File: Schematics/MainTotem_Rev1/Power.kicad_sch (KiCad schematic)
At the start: 0 parts

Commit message: Adding the MTL Schematics in post editing
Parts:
- added 3V3HPSoC: YELLOW, symbol Device:LED
- added 3V3HSSoC: GREEN, symbol Device:LED
- added 3V3SoC, GND: TestPoint, symbol Connector:TestPoint
- added C33, C36, C37, C40: 10u, symbol Device:C
- added C34, C35, C38, C39: 100n, symbol Device:C
- added C41, C43: 4.7u, symbol Device:C
- added C42, C44, C45: 0.1u, symbol Device:C
- added C46: 22u, symbol Device:C
- added R11, R12: 1k, symbol Device:R
- added R13: 56k, symbol Device:R
- added R14: 110k, symbol Device:R
- added R15: 100k, symbol Device:R
- added U5, U6: AP7361C-33Y5-13, SOT89-5_DIO, symbol LDO_ShamanLink:AP7361C-33Y5-13
- added U7: PTPS2117DRLR, SOT-5X3-8_DRL_TEX, symbol TPS2117:PTPS2117DRLR
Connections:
- new net: C35.1, C36.1, C43.1, C44.1, R11.1, U5.5 (OUT), U7.6 (VIN2)
- new net: R13.1, R14.2, U7.4 (PR1)
- new net: C39.1, C40.1, C41.1, C42.1, R12.1, R14.1, R15.1, U6.5 (OUT), U7.3 (VIN1), U7.5 (MODE)
- new net: R15.2, U7.8 (ST)
- new net: 3V3HPSoC.2 (A), R11.2
- new net: 3V3HSSoC.2 (A), R12.2
- new net 3V3MODULES: 3V3SoC.1, C45.1, C46.1, U7.2 (VOUT), U7.7 (VOUT)
- new net 5VHPSoC: C33.1, C34.1, U5.1 (EN), U5.4 (IN)
- new net 5VHSSoC: C37.1, C38.1, U6.1 (EN), U6.4 (IN)
- new net GND: 3V3HPSoC.1 (K), 3V3HSSoC.1 (K), C33.2, C34.2, C35.2, C36.2, C37.2, C38.2, C39.2, C40.2, C41.2, C42.2, C43.2, C44.2, C45.2, C46.2, GND.1, R13.2, U5.2 (GND), U6.2 (GND), U7.1 (GND)
- no-connect marks 0 -> 2
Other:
- added sheet ShamanLinkPower (ShamanLinkPower.kicad_sch)

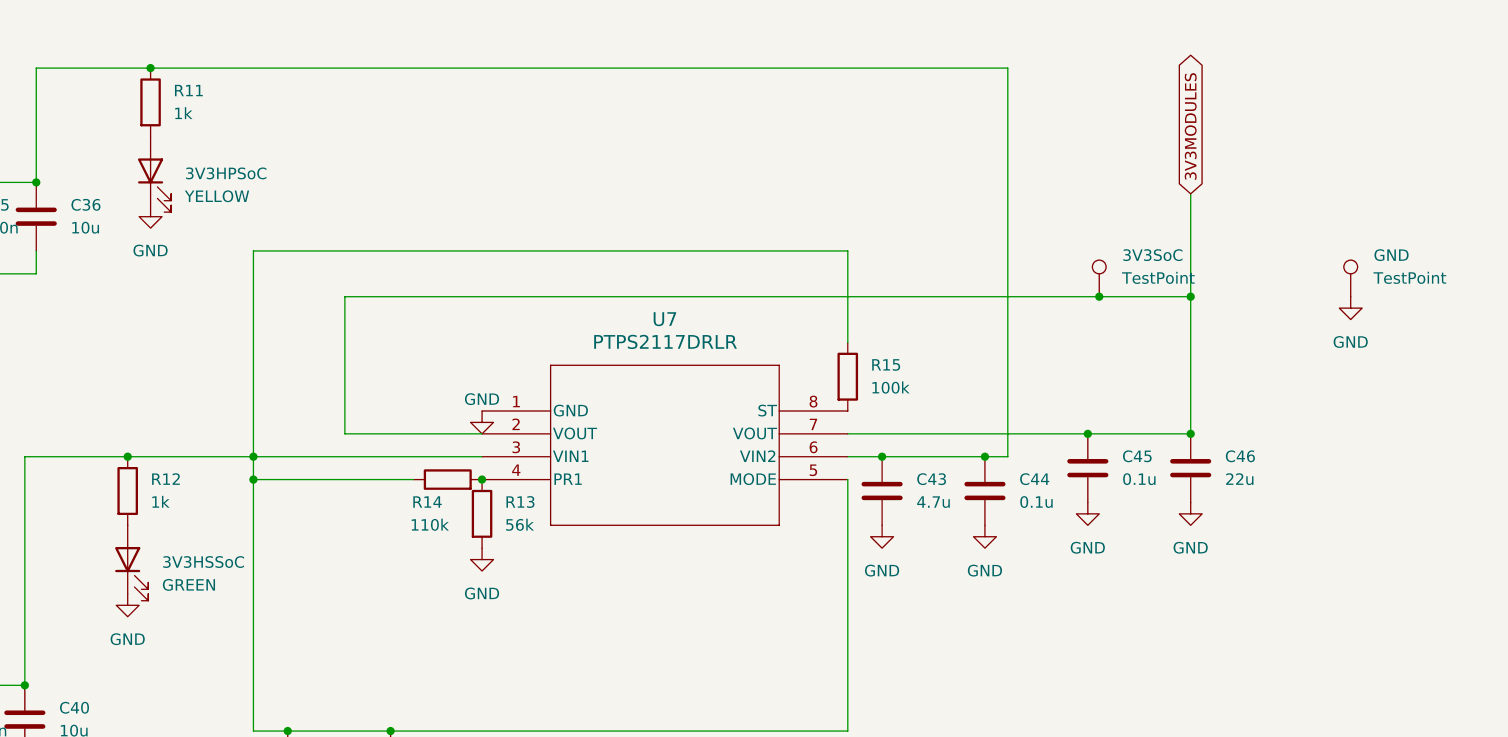
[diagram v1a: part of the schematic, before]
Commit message: Layout Edits for Mezzanine Connector routing
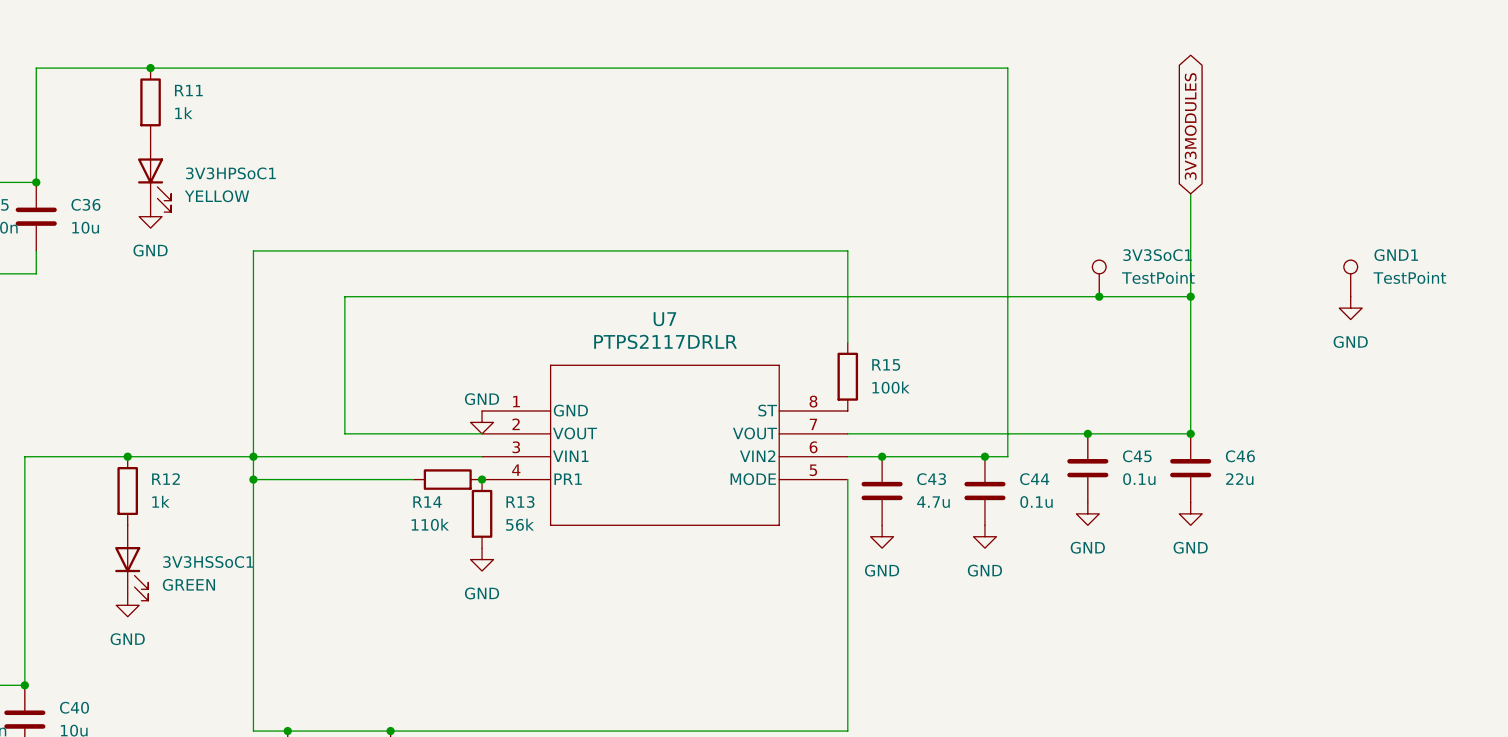
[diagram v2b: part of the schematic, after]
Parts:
- 3V3HPSoC1: renamed from 3V3HPSoC; footprint (none) -> Resistor_SMD:R_0805_2012Metric_Pad1.20x1.40mm_HandSolder
- 3V3HSSoC1: renamed from 3V3HSSoC; footprint (none) -> Resistor_SMD:R_0805_2012Metric_Pad1.20x1.40mm_HandSolder
- 3V3SoC1: renamed from 3V3SoC; footprint (none) -> TestPoint:TestPoint_Pad_1.0x1.0mm
- C33, C36, C37, C40, C46: footprint (none) -> Capacitor_SMD:C_0805_2012Metric_Pad1.18x1.45mm_HandSolder
- C34, C35, C38, C39, C41, C42, C43, C44, C45: footprint (none) -> Capacitor_SMD:C_0603_1608Metric_Pad1.08x0.95mm_HandSolder
- GND1: renamed from GND; footprint (none) -> TestPoint:TestPoint_Pad_1.0x1.0mm
- R11, R12, R13, R14, R15: footprint (none) -> Resistor_SMD:R_0603_1608Metric_Pad0.98x0.95mm_HandSolder
- U5, U6: footprint SOT89-5_DIO -> LDO_ShamanLink:SOT89-5_DIO-M
- U7: footprint SOT-5X3-8_DRL_TEX -> TPS2117:SOT-5X3-8_DRL_TEX-M
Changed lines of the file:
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@@
 			)
 		)
-		(property "Footprint" ""
+		(property "Footprint" "Capacitor_SMD:C_0603_1608Metric_Pad1.08x0.95mm_HandSolder"
 			(at 243.5352 104.14 0)
 			(effects
@@
 			)
 		)
-		(property "Footprint" ""
+		(property "Footprint" "Capacitor_SMD:C_0805_2012Metric_Pad1.18x1.45mm_HandSolder"
 			(at 254.9652 104.14 0)
 			(effects
@@
 			)
 		)
-		(property "Footprint" ""
+		(property "Footprint" "Capacitor_SMD:C_0603_1608Metric_Pad1.08x0.95mm_HandSolder"
 			(at 116.5352 76.2 0)
 			(effects
@@
 			)
 		)
-		(property "Footprint" "SOT89-5_DIO"
+		(property "Footprint" "LDO_ShamanLink:SOT89-5_DIO-M"
 			(at 63.5 66.04 0)
 			(effects
@@
 			)
 		)
-		(property "Footprint" ""
+		(property "Footprint" "Resistor_SMD:R_0603_1608Metric_Pad0.98x0.95mm_HandSolder"
 			(at 173.482 105.41 90)
 			(effects
@@
 			)
 		)
-		(property "Footprint" ""
+		(property "Footprint" "Capacitor_SMD:C_0603_1608Metric_Pad1.08x0.95mm_HandSolder"
 			(at 115.2652 132.08 0)
 			(effects
@@
 		(dnp no)
 		(fields_autoplaced yes)
-		(property "Reference" "3V3SoC"
+		(property "Reference" "3V3SoC1"
 			(at 246.38 76.7079 0)
 			(effects
@@
 			)
 		)
-		(property "Footprint" ""
+		(property "Footprint" "TestPoint:TestPoint_Pad_1.0x1.0mm"
 			(at 248.92 81.28 0)
 			(effects
@@
 			(project ""
 				(path "/f88ba0f4-041f-4cf3-b904-3ea5c6101abb/8cdda753-59d0-43d1-9f6c-24e675cc293c"
-					(reference "3V3SoC")
+					(reference "3V3SoC1")
 					(unit 1)
 				)
@@
 			)
 		)
-		(property "Footprint" ""
+		(property "Footprint" "Capacitor_SMD:C_0603_1608Metric_Pad1.08x0.95mm_HandSolder"
 			(at 220.6752 106.68 0)
 			(effects
@@
 			)
 		)
-		(property "Footprint" ""
+		(property "Footprint" "Resistor_SMD:R_0603_1608Metric_Pad0.98x0.95mm_HandSolder"
 			(at 214.122 90.17 90)
 			(effects
@@
 			)
 		)
-		(property "Footprint" "SOT89-5_DIO"
+		(property "Footprint" "LDO_ShamanLink:SOT89-5_DIO-M"
 			(at 62.23 121.92 0)
 			(effects
@@
 			)
 		)
-		(property "Footprint" "SOT-5X3-8_DRL_TEX"
+		(property "Footprint" "TPS2117:SOT-5X3-8_DRL_TEX-M"
 			(at 175.26 93.98 0)
 			(effects
@@
 			)
 		)
-		(property "Footprint" ""
+		(property "Footprint" "Capacitor_SMD:C_0603_1608Metric_Pad1.08x0.95mm_HandSolder"
 			(at 232.1052 106.68 0)
 			(effects
@@
 			)
 		)
-		(property "Footprint" ""
+		(property "Footprint" "Capacitor_SMD:C_0603_1608Metric_Pad1.08x0.95mm_HandSolder"
 			(at 166.0652 137.16 0)
 			(effects
@@
 			)
 		)
-		(property "Footprint" ""
+		(property "Footprint" "Capacitor_SMD:C_0603_1608Metric_Pad1.08x0.95mm_HandSolder"
 			(at 75.8952 85.09 0)
 			(effects
@@
 			)
 		)
-		(property "Footprint" ""
+		(property "Footprint" "Capacitor_SMD:C_0805_2012Metric_Pad1.18x1.45mm_HandSolder"
 			(at 65.7352 85.09 0)
 			(effects
@@
 			)
 		)
-		(property "Footprint" ""
+		(property "Footprint" "Resistor_SMD:R_0603_1608Metric_Pad0.98x0.95mm_HandSolder"
 			(at 171.45 103.378 90)
 			(effects
@@
 			)
 		)
-		(property "Footprint" ""
+		(property "Footprint" "Capacitor_SMD:C_0805_2012Metric_Pad1.18x1.45mm_HandSolder"
 			(at 64.4652 140.97 0)
 			(effects
@@
 			)
 		)
-		(property "Footprint" ""
+		(property "Footprint" "Capacitor_SMD:C_0603_1608Metric_Pad1.08x0.95mm_HandSolder"
 			(at 74.6252 140.97 0)
 			(effects
@@
 		(dnp no)
 		(fields_autoplaced yes)
-		(property "Reference" "3V3HPSoC"
+		(property "Reference" "3V3HPSoC1"
 			(at 142.24 67.6274 90)
 			(effects
@@
 			)
 		)
-		(property "Footprint" ""
+		(property "Footprint" "Resistor_SMD:R_0805_2012Metric_Pad1.20x1.40mm_HandSolder"
 			(at 138.43 67.31 0)
 			(effects
@@
 			(project ""
 				(path "/f88ba0f4-041f-4cf3-b904-3ea5c6101abb/8cdda753-59d0-43d1-9f6c-24e675cc293c"
-					(reference "3V3HPSoC")
+					(reference "3V3HPSoC1")
 					(unit 1)
 				)
@@
 		(dnp no)
 		(fields_autoplaced yes)
-		(property "Reference" "3V3HSSoC"
+		(property "Reference" "3V3HSSoC1"
 			(at 139.7 110.8074 90)
 			(effects
@@
 			)
 		)
-		(property "Footprint" ""
+		(property "Footprint" "Resistor_SMD:R_0805_2012Metric_Pad1.20x1.40mm_HandSolder"
 			(at 135.89 110.49 0)
 			(effects
@@
 			(project ""
 				(path "/f88ba0f4-041f-4cf3-b904-3ea5c6101abb/8cdda753-59d0-43d1-9f6c-24e675cc293c"
-					(reference "3V3HSSoC")
+					(reference "3V3HSSoC1")
 					(unit 1)
 				)
@@
 			)
 		)
-		(property "Footprint" ""
+		(property "Footprint" "Resistor_SMD:R_0603_1608Metric_Pad0.98x0.95mm_HandSolder"
 			(at 136.652 59.69 90)
 			(effects
@@
 			)
 		)
-		(property "Footprint" ""
+		(property "Footprint" "Capacitor_SMD:C_0805_2012Metric_Pad1.18x1.45mm_HandSolder"
 			(at 125.4252 132.08 0)
 			(effects
@@
 		(dnp no)
 		(fields_autoplaced yes)
-		(property "Reference" "GND"
+		(property "Reference" "GND1"
 			(at 274.32 76.7079 0)
 			(effects
@@
 			)
 		)
-		(property "Footprint" ""
+		(property "Footprint" "TestPoint:TestPoint_Pad_1.0x1.0mm"
 			(at 276.86 81.28 0)
 			(effects
@@
 			(project "MainTotem_Rev1"
 				(path "/f88ba0f4-041f-4cf3-b904-3ea5c6101abb/8cdda753-59d0-43d1-9f6c-24e675cc293c"
-					(reference "GND")
+					(reference "GND1")
 					(unit 1)
 				)
@@
 			)
 		)
-		(property "Footprint" ""
+		(property "Footprint" "Capacitor_SMD:C_0805_2012Metric_Pad1.18x1.45mm_HandSolder"
 			(at 126.6952 76.2 0)
 			(effects
@@
 			)
 		)
-		(property "Footprint" ""
+		(property "Footprint" "Resistor_SMD:R_0603_1608Metric_Pad0.98x0.95mm_HandSolder"
 			(at 134.112 102.87 90)
 			(effects
@@
 			)
 		)
-		(property "Footprint" ""
+		(property "Footprint" "Capacitor_SMD:C_0603_1608Metric_Pad1.08x0.95mm_HandSolder"
 			(at 154.6352 137.16 0)
 			(effects
